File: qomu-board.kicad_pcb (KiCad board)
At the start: 6 copper layers, 28.1 x 10.7 mm, 61 parts, among them IC1 EOS-S3, J1 FTSH-105-01-L-DV-K, J2 825437-4, J3 22-23-2021, Q1 RV1C002UN, Q2 RV1C002UN, Q3 RV1C002UN, SW2 Captouch Pads, U1 MIC5504-3.3YMT, U10 UHD1110-FKA, U2 MIC5504-3.3YMT, U4 GD25Q16CEIGR, U5 MC3635, U9 USB-B

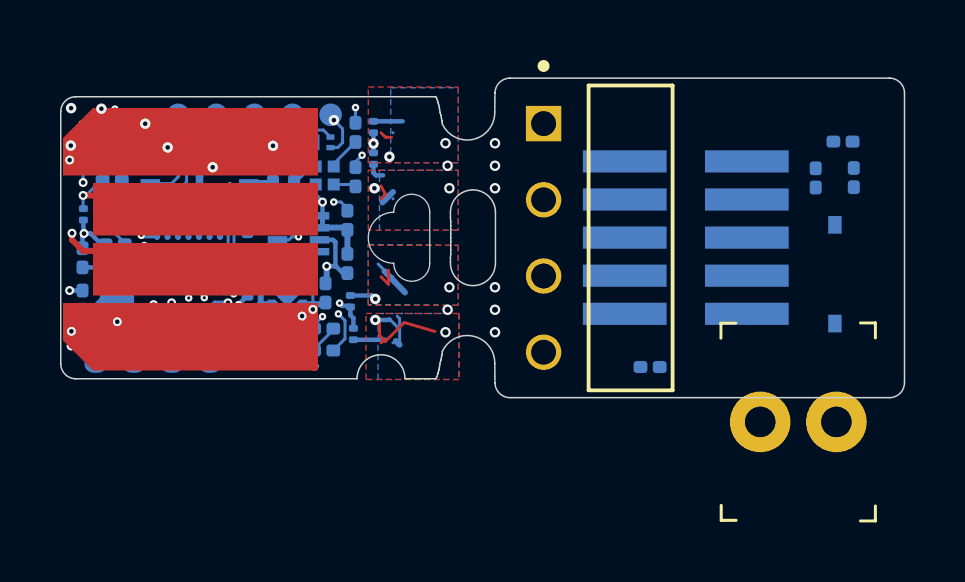
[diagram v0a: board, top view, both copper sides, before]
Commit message: Removed soldermask from TOUCHx pads
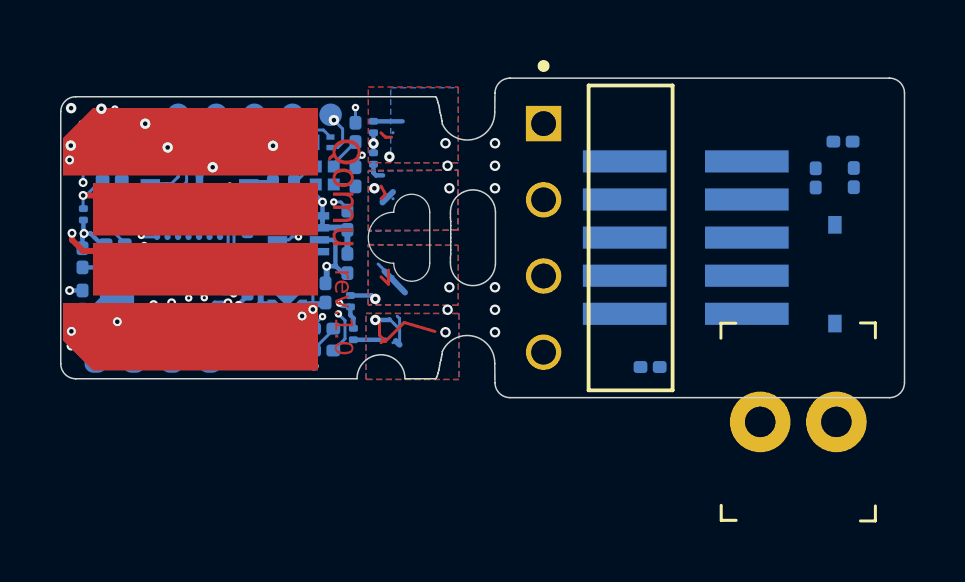
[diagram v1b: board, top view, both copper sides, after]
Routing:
- net /RST_N: track 6.56 -> 23.0 mm, vias 2 -> 5
- net /C1: track 4.75 -> 18.2 mm, vias 2 -> 5
- net +3V3: track 27.2 -> 33.9 mm, vias 23 -> 24
- net GND: track 33.6 -> 38.2 mm
- added copper zone on B.Cu, net (none)
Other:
- board text added: "Qomu"
- board text added: "rev.1.0"

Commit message: Routing completed
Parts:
- added S1: MSS3-V-T_R, qomu-board-footprints:Switch_Slide_MSS3, B.Cu at (43.5, 22.2)
- D8: footprint qomu-board-footprints:SOD-323 -> qomu-board-footprints:SOD-323-SD05
- J3: value 22-23-2021 -> MC-HVT1-S02-G; footprint qomu-board-footprints:PinHeader_1x2_P2.54mm_Drill1.02mm -> qomu-board-footprints:PinHeader_1x2_P1.27mm_Drill.7mm_with_622002115121_plug; moved to B.Cu
- moved J3 10.2 mm to (40.6, 18.0)
- moved D8 8.29 mm to (36.2, 18.0), turned to 0 degrees
- moved C12 8.23 mm to (34.1, 18.3)
- moved R6 4.58 mm to (41.2, 26.0), turned to 90 degrees
- moved R13 2.45 mm to (42.7, 17.5), turned to 180 degrees
- moved R15 1.57 mm to (44.2, 17.5)
- moved J1 1.48 mm to (37.1, 23.1), turned to 0 degrees
- moved J2 0.32 mm to (32.8, 18.0)
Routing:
- net +3V3: track 33.9 -> 57.4 mm, vias 24 -> 28
- net /SWD_IO: track 13.7 -> 32.0 mm, vias 1 -> 3
- net /SWD_CLK: track 13.1 -> 30.7 mm, vias 1 -> 3
- net GND: track 38.2 -> 49.8 mm, vias 49 -> 57
- net /C1: track 18.2 -> 29.4 mm, vias 5 -> 6
- net Net-(J3-Pad2): track 0.00 -> 10.1 mm
- net /RST_N: track 23.0 -> 33.1 mm, vias 5 -> 6
- net /UART_RX: track 11.8 -> 17.7 mm
- net Net-(J1-Pad8): track 0.00 -> 1.72 mm, vias 0 -> 1
- net Net-(J1-Pad7): track 0.00 -> 1.72 mm, vias 0 -> 1
- net Net-(J1-Pad6): track 0.00 -> 1.72 mm, vias 0 -> 1
- net /UART_TX: track 11.6 -> 12.7 mm

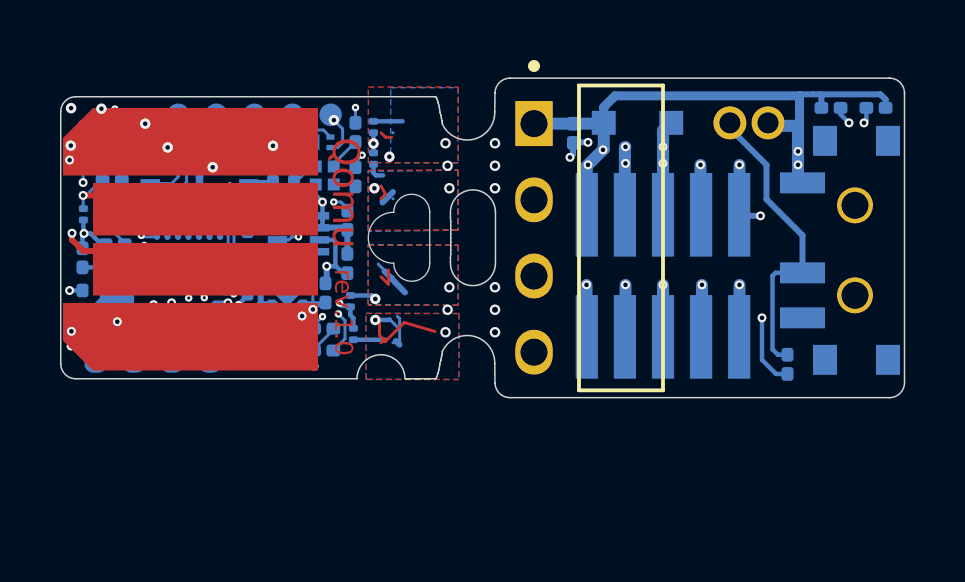
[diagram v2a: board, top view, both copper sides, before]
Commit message: Resolved DRC errors
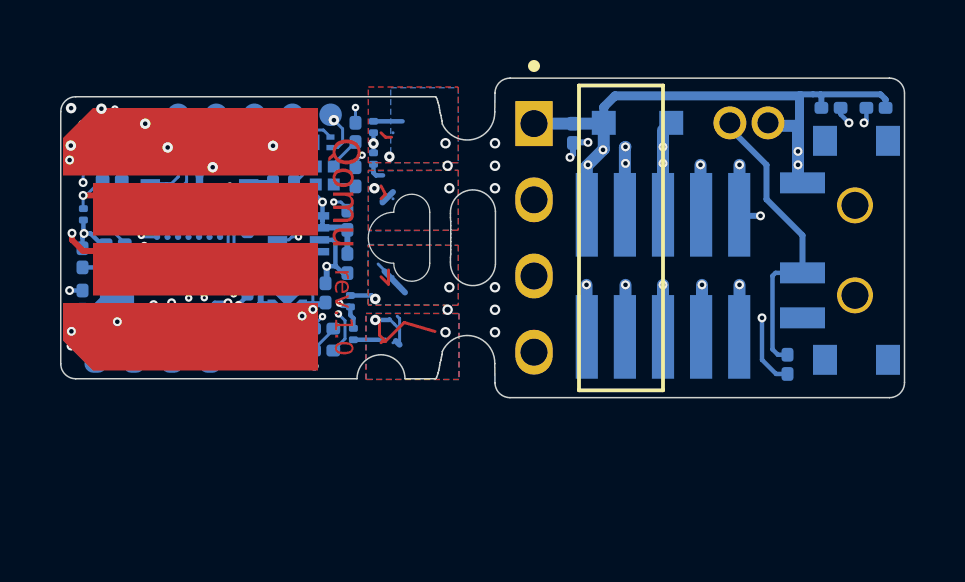
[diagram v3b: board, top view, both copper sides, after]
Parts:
- U5: footprint qomu-board:MC3635 -> qomu-board-footprints:MC3635
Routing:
- added copper zone on In3.Cu, net GND
- removed copper zone on B.Cu, net (none)
- removed copper zone on GND.Cu, net GND

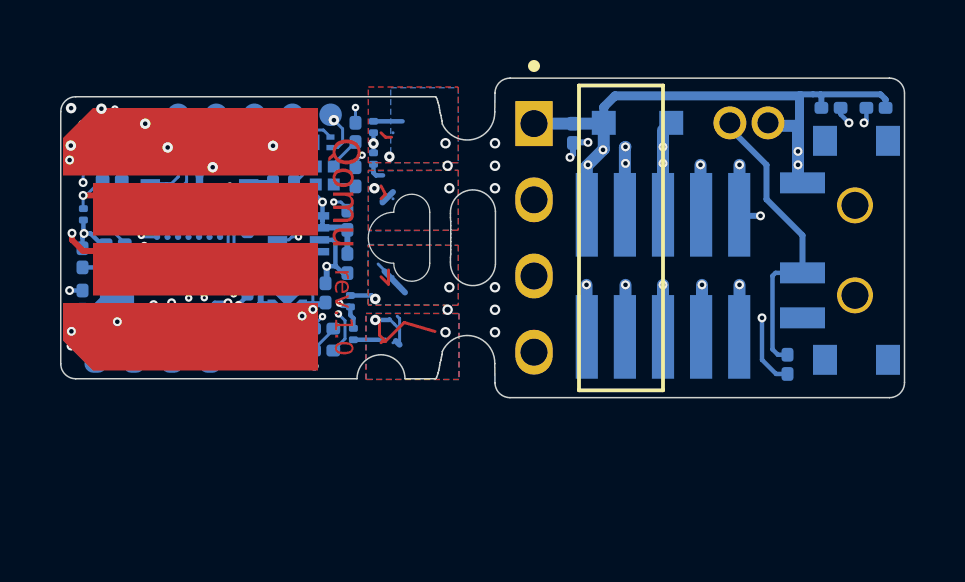
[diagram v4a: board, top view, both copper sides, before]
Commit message: Added optional jumpers to enable UART TX/RX on unassigned J1 pins
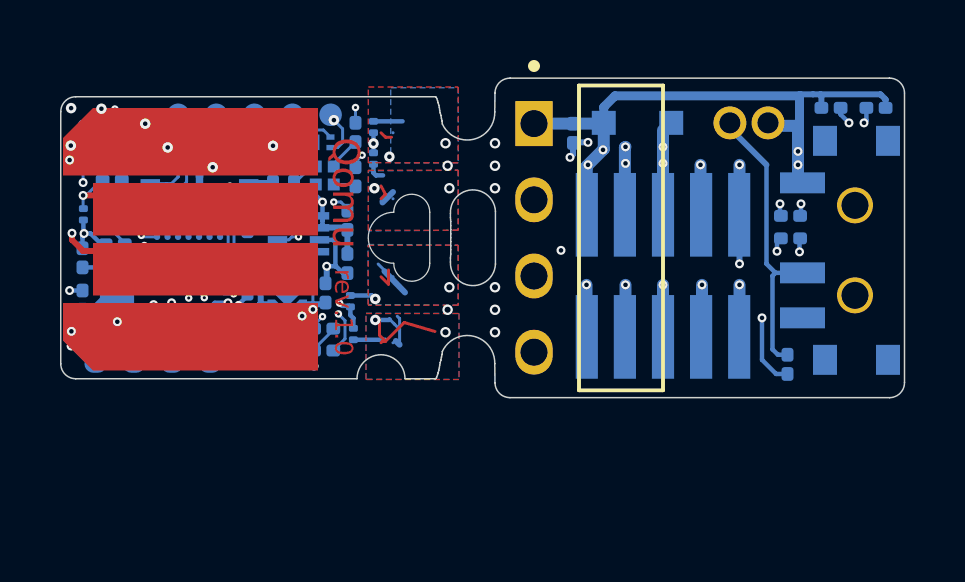
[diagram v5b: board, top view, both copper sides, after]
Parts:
- added R10: 0R, qomu-board-footprints:R_0201_0603Metric, B.Cu at (41.4, 21.8)
- added R7: 0R, qomu-board-footprints:R_0201_0603Metric, B.Cu at (41.4, 21.1)
- U5: footprint qomu-board-footprints:MC3635 -> qomu-board:MC3635
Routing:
- net /UART_TX: track 12.7 -> 23.1 mm, vias 1 -> 3
- net /UART_RX: track 17.7 -> 26.6 mm, vias 1 -> 2
- net Net-(J1-Pad6): track 1.72 -> 8.66 mm, vias 1 -> 2
- net Net-(J1-Pad8): track 1.72 -> 6.56 mm, vias 1 -> 2
- net /SWD_CLK: track 30.7 -> 34.1 mm
- net /SWD_IO: track 32.0 -> 34.8 mm
- net GND: track 49.8 -> 50.8 mm

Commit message: Pin swaps implemented on PCB
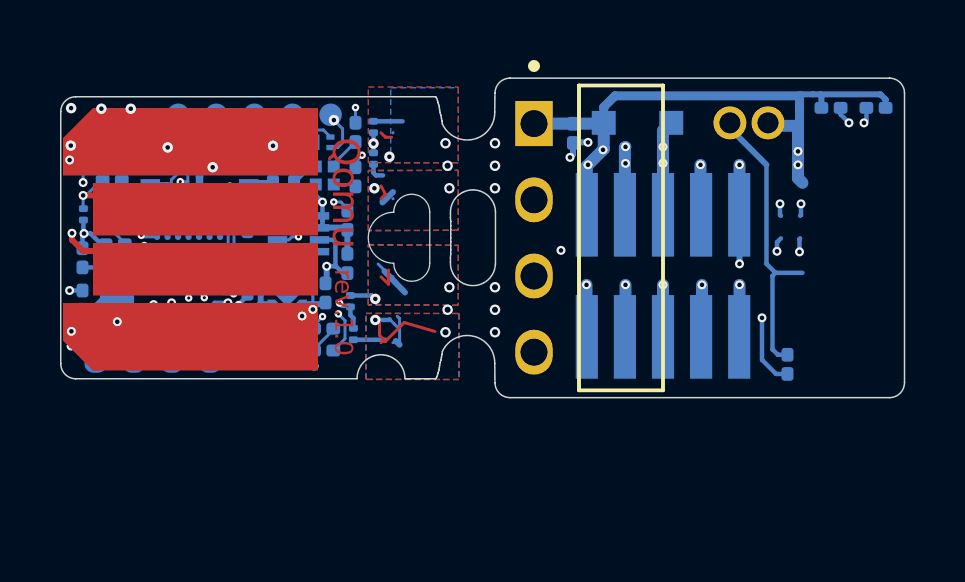
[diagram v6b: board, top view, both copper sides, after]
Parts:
- removed R10, R7: 0R, qomu-board-footprints:R_0201_0603Metric
- removed S1: MSS3-V-T_R, qomu-board-footprints:Switch_Slide_MSS3
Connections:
- IC1 pad A6: /TOUCH_2 -> /LED_G
- IC1 pad D3: /LED_G -> /TOUCH_2
- IC1 pad E3: /R_USB_P -> /TOUCH_4
- IC1 pad E4: /TOUCH_4 -> /R_USB_P
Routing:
- net /LED_G: track 7.08 -> 13.2 mm, vias 4 -> 8
- net /TOUCH_2: track 13.2 -> 18.0 mm, vias 2 -> 5
- net Net-(Q1-Pad3): track 12.5 -> 10.2 mm
- net GND: track 50.8 -> 52.0 mm
- net Net-(Q2-Pad3): track 10.1 -> 8.95 mm
- net /R_USB_P: track 3.48 -> 4.22 mm
- net /TOUCH_4: track 11.5 -> 12.2 mm, vias 2 -> 4

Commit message: Testpoint on F2 added
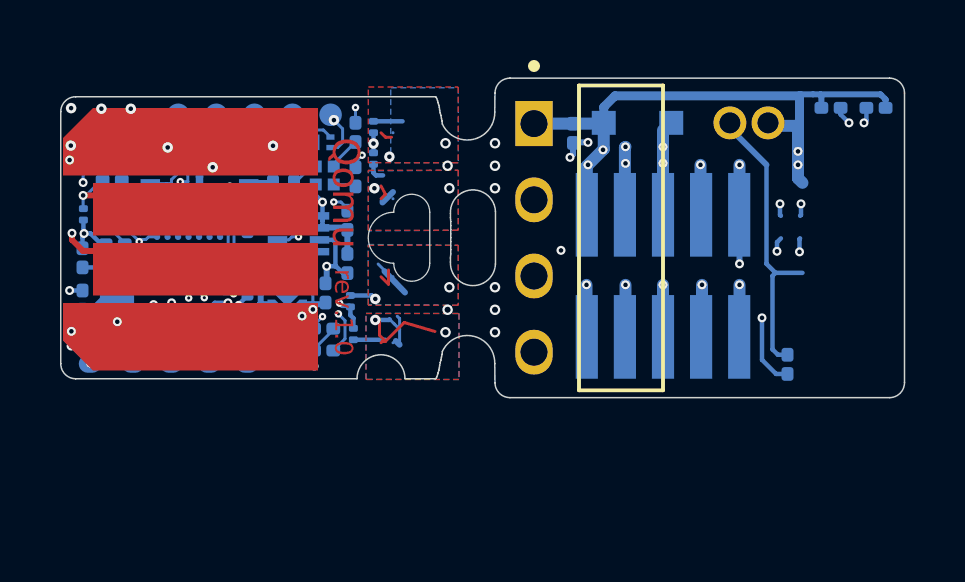
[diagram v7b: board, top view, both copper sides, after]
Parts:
- added TP10: TP_SMD_0_75MM, qomu-board-footprints:Testpoint_smd_0_75_0_6mm, B.Cu at (20.7, 28.0)
- moved TP2 3.78 mm to (23.2, 25.9)
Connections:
- net Net-(IC1-PadE1) renamed /E1
- IC1 pad F2: Net-(IC1-PadF2) -> /F2
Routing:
- net /E1: track 4.80 -> 12.5 mm
- net /F2: track 0.00 -> 6.42 mm, vias 0 -> 2
- net GND: track 52.0 -> 52.8 mm
- net /C1: track 29.4 -> 28.7 mm

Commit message: R7,R10,S1 options restored. Library link fixed
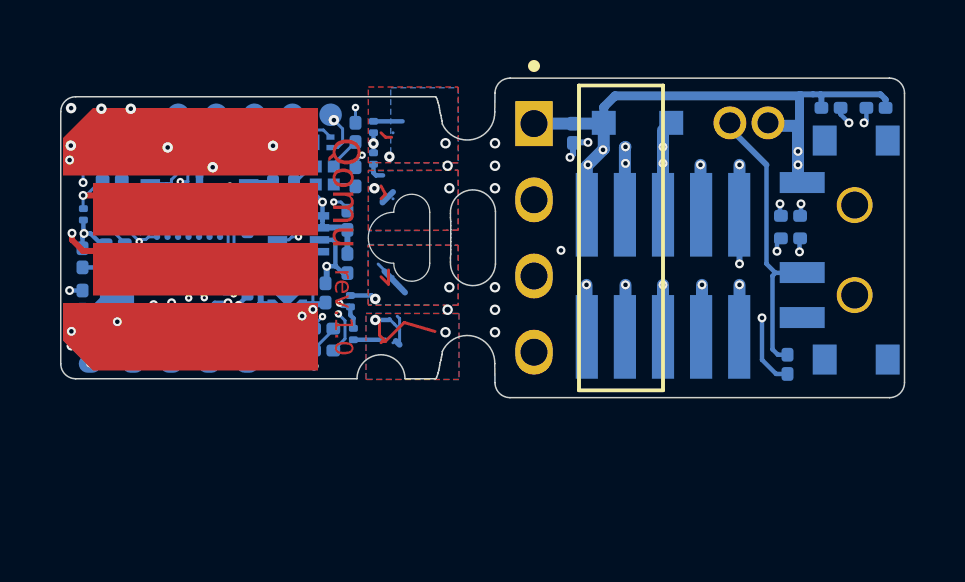
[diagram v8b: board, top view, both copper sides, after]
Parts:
- added R10: 0R, qomu-board-footprints:R_0201_0603Metric, B.Cu at (41.4, 21.8)
- added R7: 0R, qomu-board-footprints:R_0201_0603Metric, B.Cu at (41.4, 21.1)
- added S1: MSS3-V-T_R, qomu-board-footprints:Switch_Slide_MSS3, B.Cu at (43.5, 22.2)
